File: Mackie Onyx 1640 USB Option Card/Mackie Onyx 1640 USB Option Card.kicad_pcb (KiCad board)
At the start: 2 copper layers, 5 parts, among them J1 Conn_02x17_Odd_Even, U1 XU316-1024-QF60B-C24, U2 CS5368-CQZ, U3 CS5368-CQZ, U4 CS5368-CQZ

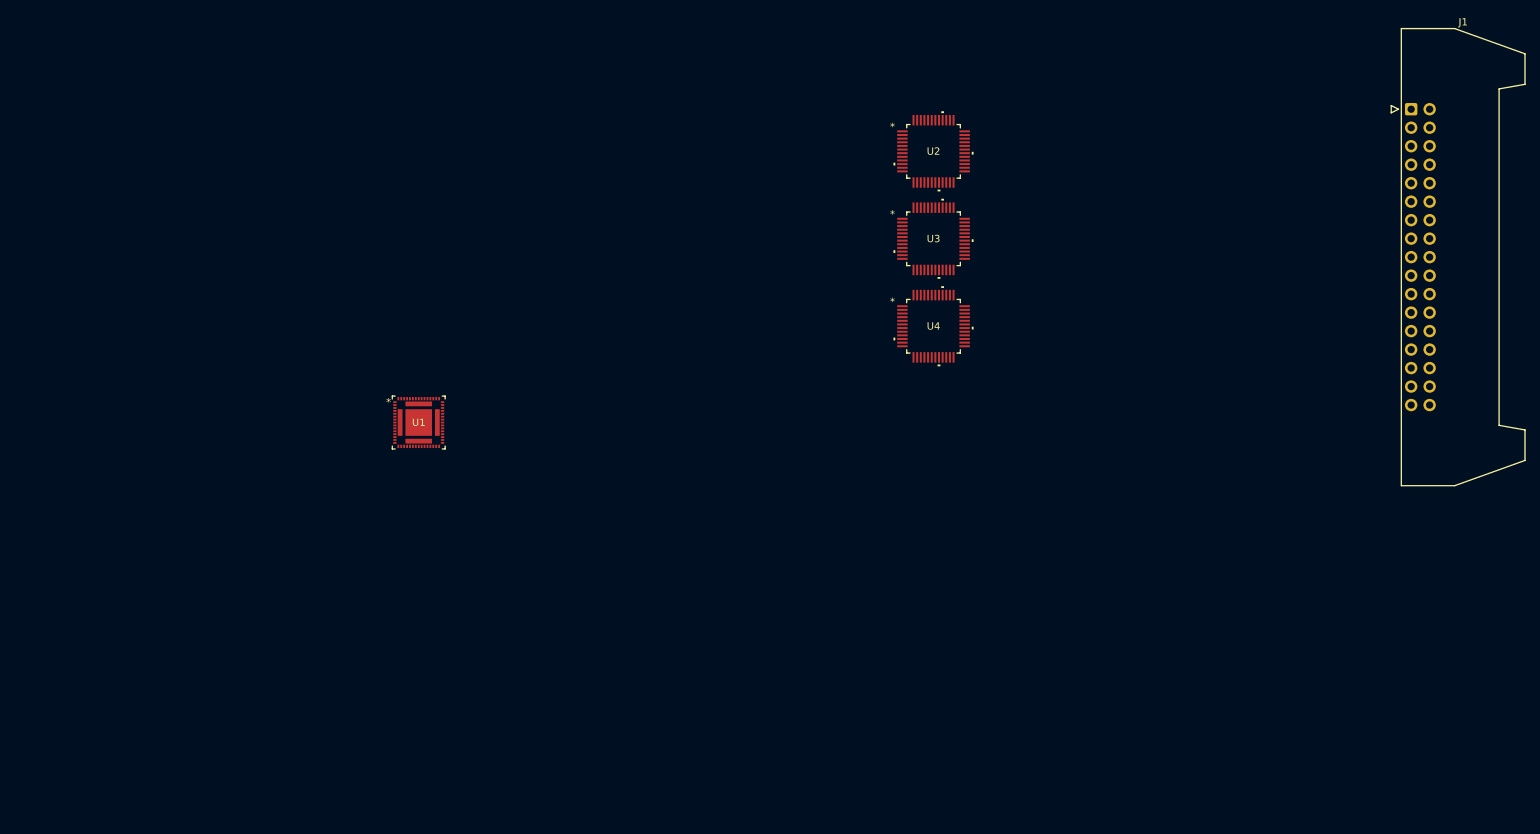
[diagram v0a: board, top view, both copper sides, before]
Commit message: Added board dimensions and connector position
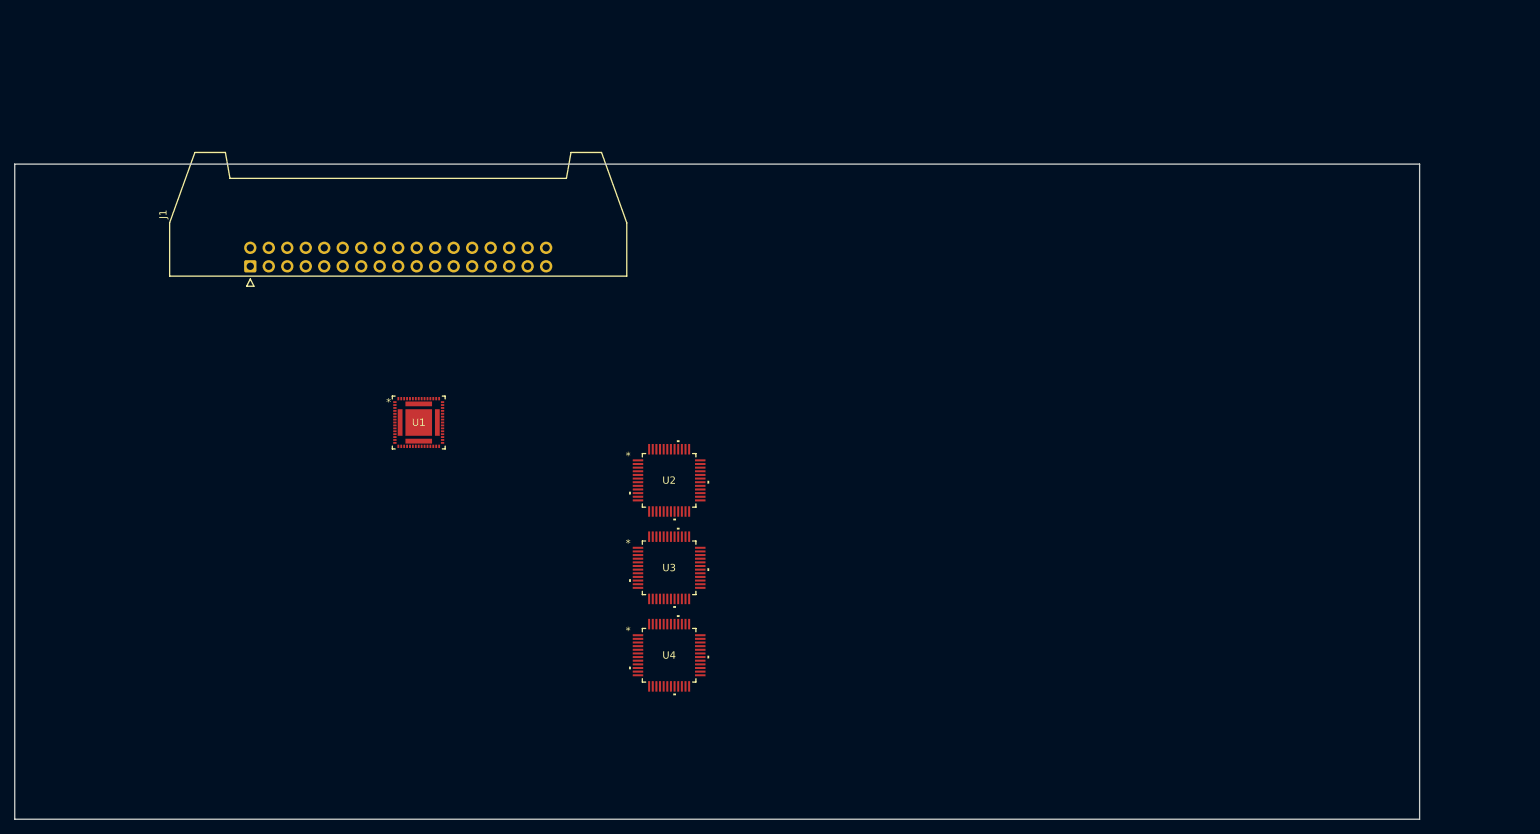
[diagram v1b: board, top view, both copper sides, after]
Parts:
- moved J1 160.9 mm to (82.4, 64.0), turned to 90 degrees
- moved U2 58.0 mm to (139.9, 93.4)
- moved U4 58.0 mm to (139.9, 117.5)
- moved U3 58.0 mm to (139.9, 105.5)
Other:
- board outline added: 193 x 90 mm

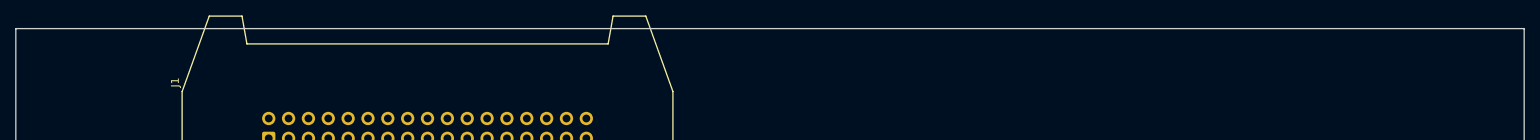
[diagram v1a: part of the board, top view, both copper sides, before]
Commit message: Added mounting holes (where gold posts are on firewire card) assumed them to be M3.5 cus that's what came closest from measuring screws (assume Placeholder)
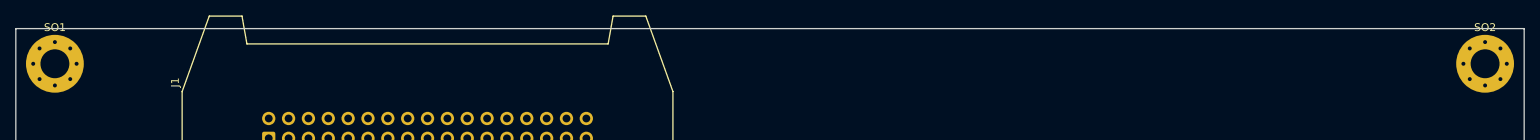
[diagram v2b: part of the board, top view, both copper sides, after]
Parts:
- added SO1: MountingHole_3.7mm_Pad_Via, MountingHole:MountingHole_3.7mm_Pad_Via, F.Cu at (55.0, 54.5)
- added SO2: MountingHole_3.7mm_Pad_Via, MountingHole:MountingHole_3.7mm_Pad_Via, F.Cu at (238.0, 54.5)
